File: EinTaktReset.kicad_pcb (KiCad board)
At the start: 2 copper layers, 34 parts, among them P10 CONN_01X01, P11 CONN_01X01, P12 CONN_01X01, P13 CONN_01X01, P14 CONN_01X01, P15 CONN_01X01, P2 CONN_01X01, P3 CONN_01X01, P4 CONN_02X10, P5 CONN_01X01, P6 CONN_01X01, P7 CONN_01X01, P8 CONN_01X01, P9 CONN_01X01, U2 74540En, U3 74HCT541_PWR

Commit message: footprinting EintaktReset3
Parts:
- added C3: 220 µ, Capacitors_ThroughHole:CP_Radial_D8.0mm_P3.50mm, F.Cu at (224.3, 28.2)
- added C4: 220µ, Capacitors_ThroughHole:CP_Radial_D8.0mm_P3.50mm, F.Cu at (233.4, 28.2)
- added C5: 10n, Capacitors_ThroughHole:C_Disc_D3.0mm_W1.6mm_P2.50mm, F.Cu at (206.4, 32.6)
- added D2: LED, LEDs:LED_D5.0mm, F.Cu at (200.4, 34.5)
- added DROT1: LED, LEDs:LED_D3.0mm, F.Cu at (250.3, 25.9)
- added P1: CONN_02X10, Pin_Headers:Pin_Header_Straight_2x10_Pitch2.00mm, F.Cu at (214.3, 3.02)
- added RV1: POT, Potentiometers:Potentiometer_Trimmer_Piher_PT-10v5_Horizontal_Px5.0mm_Py5.0mm, F.Cu at (213.3, 34.0)
- added SW10: SPST, tg_foodprint:eintakt_tg_SW_CuK_JS202011CQN_DPDT_Straight, F.Cu at (317.0, 11.1)
- added SW11: SPST, tg_foodprint:eintakt_tg_SW_CuK_JS202011CQN_DPDT_Straight, F.Cu at (325.2, 4.77)
- added SW12: SPST, tg_foodprint:eintakt_tg_SW_CuK_JS202011CQN_DPDT_Straight, F.Cu at (317.0, 17.4)
- added SW13: SPST, tg_foodprint:eintakt_tg_SW_CuK_JS202011CQN_DPDT_Straight, F.Cu at (325.2, 11.1)
- added SW5: SPST, tg_foodprint:eintakt_tg_SW_CuK_JS202011CQN_DPDT_Straight, F.Cu at (308.9, 4.77)
- added SW6: SWITCH_INV, Buttons_Switches_ThroughHole:SW_TH_Tactile_Omron_B3F-10xx, F.Cu at (241.1, 25.0)
- added SW7: SPST, tg_foodprint:eintakt_tg_SW_CuK_JS202011CQN_DPDT_Straight, F.Cu at (308.9, 11.1)
- added SW8: SPST, tg_foodprint:eintakt_tg_SW_CuK_JS202011CQN_DPDT_Straight, F.Cu at (317.0, 4.77)
- added SW9: SPST, tg_foodprint:eintakt_tg_SW_CuK_JS202011CQN_DPDT_Straight, F.Cu at (308.9, 17.4)
- added U1: 74LS132, Housings_DIP:DIP-14_W7.62mm_Socket_LongPads, F.Cu at (222.2, 3.29)
- added U10: 74LS00, Housings_DIP:DIP-14_W7.62mm_Socket_LongPads, F.Cu at (255.6, 3.29)
- added U4: 74LS32, Housings_DIP:DIP-20_W7.62mm_Socket_LongPads, F.Cu at (200.4, 3.29)
- added U5: 74LS00, Housings_DIP:DIP-14_W7.62mm_Socket_LongPads, F.Cu at (276.8, 3.29)
- added U6: 74LS132, Housings_DIP:DIP-14_W7.62mm_Socket_LongPads, F.Cu at (287.9, 3.29)
- added U8: 74LS32, Housings_DIP:DIP-14_W7.62mm_Socket_LongPads, F.Cu at (233.3, 3.29)
- added U9: 74LS32, Housings_DIP:DIP-14_W7.62mm_Socket_LongPads, F.Cu at (244.5, 3.29)

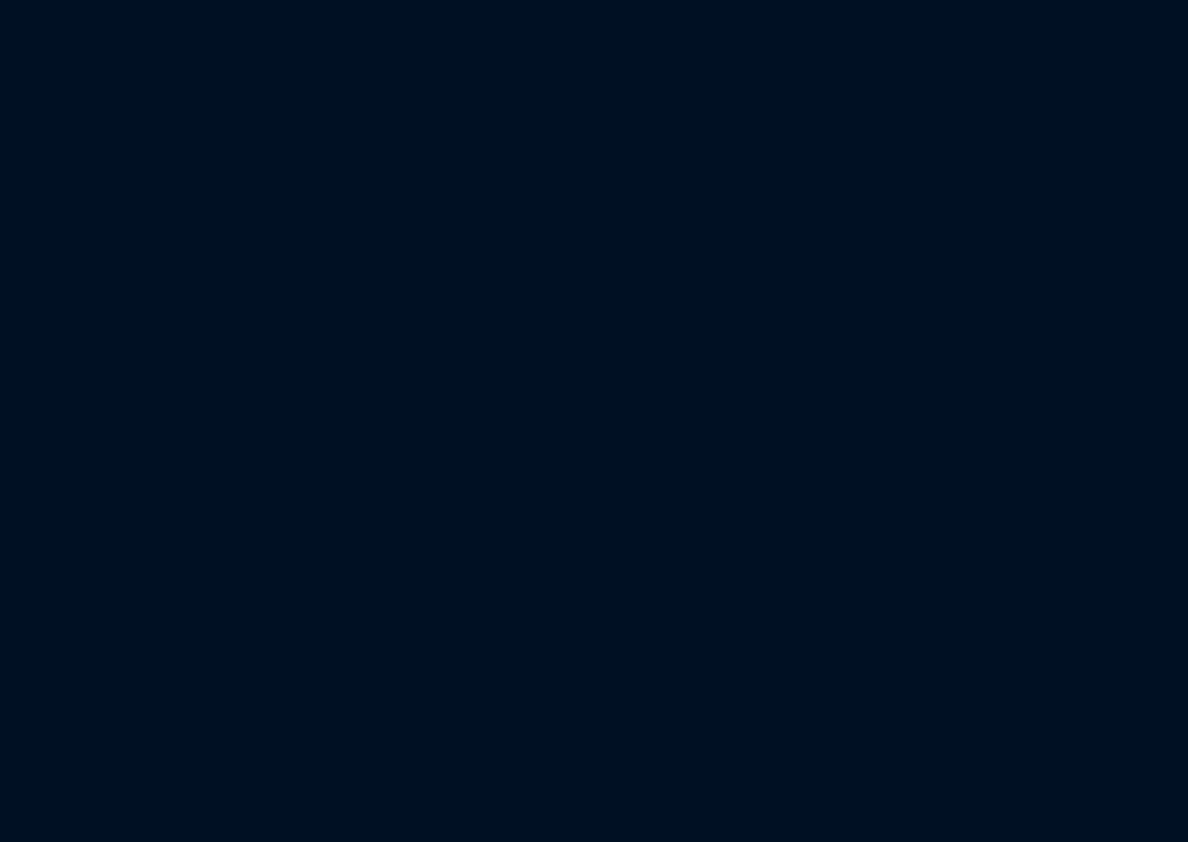
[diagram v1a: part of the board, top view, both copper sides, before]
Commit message: footprint IC1 ls624 VCO 14 pin
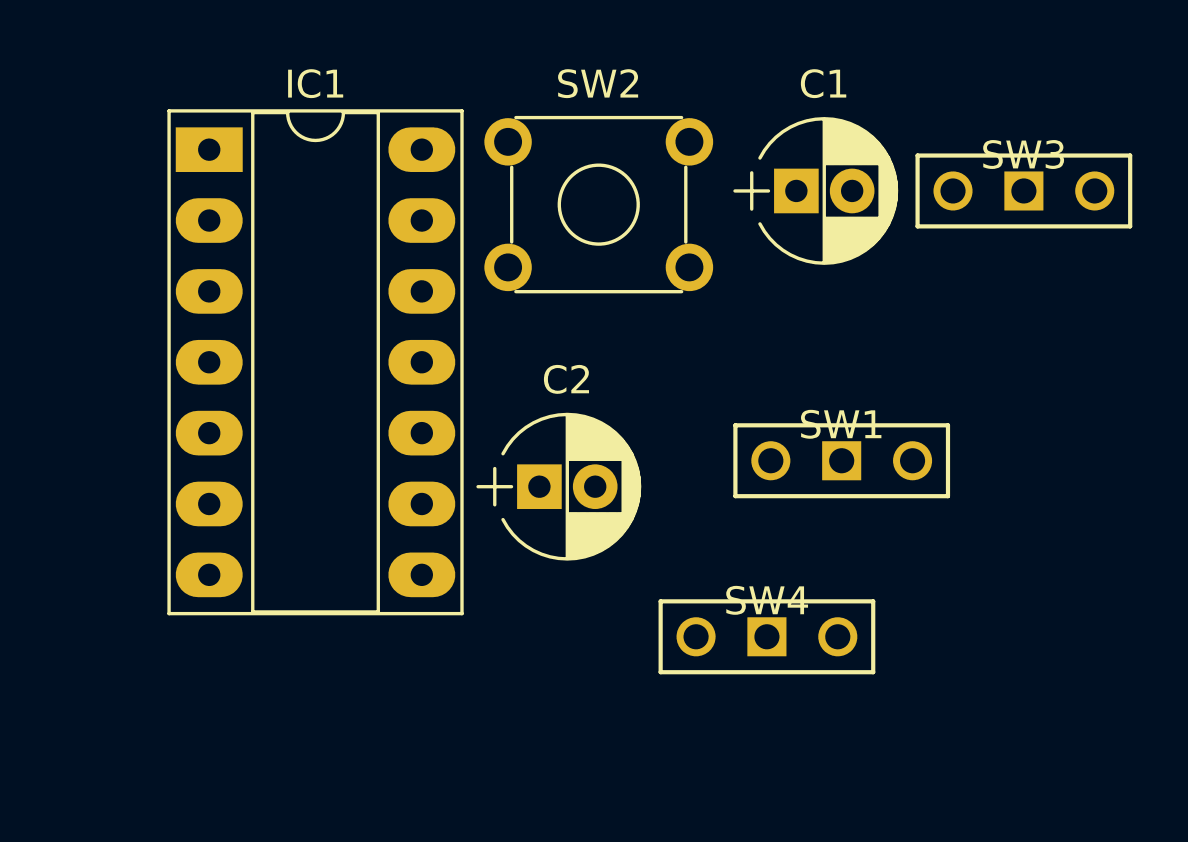
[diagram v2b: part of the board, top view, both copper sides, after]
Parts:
- added C1: 47µ, Capacitors_ThroughHole:CP_Radial_D5.0mm_P2.00mm, F.Cu at (364.6, 4.77)
- added C2: 10 µ, Capacitors_ThroughHole:CP_Radial_D5.0mm_P2.00mm, F.Cu at (355.4, 15.4)
- added IC1: 74LS624, Housings_DIP:DIP-14_W7.62mm_Socket_LongPads, F.Cu at (343.6, 3.29)
- added SW1: SPST, tg_foodprint:eintakt_tg_SW_CuK_JS202011CQN_DPDT_Straight, F.Cu at (363.7, 14.4)
- added SW2: SWITCH_INV, Buttons_Switches_ThroughHole:SW_TH_Tactile_Omron_B3F-10xx, F.Cu at (354.3, 3.01)
- added SW3: SPST, tg_foodprint:eintakt_tg_SW_CuK_JS202011CQN_DPDT_Straight, F.Cu at (370.3, 4.77)
- added SW4: SPST, tg_foodprint:eintakt_tg_SW_CuK_JS202011CQN_DPDT_Straight, F.Cu at (361.0, 20.7)

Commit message: footprint d1 smal diode do35 added
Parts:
- added D1: D, Diodes_ThroughHole:D_DO-35_SOD27_P7.62mm_Horizontal, F.Cu at (388.2, 3.02)
- moved P4 50.6 mm to (38.1, 54.6)
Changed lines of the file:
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@@
     (tracks 0)
     (zones 0)
-    (modules 64)
+    (modules 65)
     (nets 63)
   )
@@
   )
   (module Connect:1pin (layer F.Cu)
-    (at 36.468333 4.0055)
+    (at 38.1 54.61)
     (descr "module 1 pin (ou trou mecanique de percage)")
     (tags DEV)
@@
       (rotate (xyz 0 0 0))
     )
+  )
+  (module Diodes_ThroughHole:D_DO-35_SOD27_P7.62mm_Horizontal (layer F.Cu)
+    (at 388.158347 3.0175)
+    (descr "D, DO-35_SOD27 series, Axial, Horizontal, pin pitch=7.62mm, , length*diameter=4*2mm^2, , http://www.diodes.com/_files/packages/DO-35.pdf")
+    (tags "D DO-35_SOD27 series Axial Horizontal pin pitch 7.62mm  length 4mm diameter 2mm")
+    (fp_text reference D1 (at 3.81 -2.06) (layer F.SilkS)
+      (effects (font (size 1 1) (thickness 0.15)))
+    )
+    (fp_text value D (at 3.81 2.06) (layer F.Fab)
+      (effects (font (size 1 1) (thickness 0.15)))
+    )
+    (fp_line (start 8.7 -1.35) (end -1.05 -1.35) (layer F.CrtYd) (width 0.05))
+    (fp_line (start 8.7 1.35) (end 8.7 -1.35) (layer F.CrtYd) (width 0.05))
+    (fp_line (start -1.05 1.35) (end 8.7 1.35) (layer F.CrtYd) (width 0.05))
+    (fp_line (start -1.05 -1.35) (end -1.05 1.35) (layer F.CrtYd) (width 0.05))
+    (fp_line (start 2.41 -1.06) (end 2.41 1.06) (layer F.SilkS) (width 0.12))
+    (fp_line (start 6.64 0) (end 5.87 0) (layer F.SilkS) (width 0.12))
+    (fp_line (start 0.98 0) (end 1.75 0) (layer F.SilkS) (width 0.12))
+    (fp_line (start 5.87 -1.06) (end 1.75 -1.06) (layer F.SilkS) (width 0.12))
+    (fp_line (start 5.87 1.06) (end 5.87 -1.06) (layer F.SilkS) (width 0.12))
+    (fp_line (start 1.75 1.06) (end 5.87 1.06) (layer F.SilkS) (width 0.12))
+    (fp_line (start 1.75 -1.06) (end 1.75 1.06) (layer F.SilkS) (width 0.12))
+    (fp_line (start 2.41 -1) (end 2.41 1) (layer F.Fab) (width 0.1))
+    (fp_line (start 7.62 0) (end 5.81 0) (layer F.Fab) (width 0.1))
+    (fp_line (start 0 0) (end 1.81 0) (layer F.Fab) (width 0.1))
+    (fp_line (start 5.81 -1) (end 1.81 -1) (layer F.Fab) (width 0.1))
+    (fp_line (start 5.81 1) (end 5.81 -1) (layer F.Fab) (width 0.1))
+    (fp_line (start 1.81 1) (end 5.81 1) (layer F.Fab) (width 0.1))
+    (fp_line (start 1.81 -1) (end 1.81 1) (layer F.Fab) (width 0.1))
+    (fp_text user %R (at 3.81 0) (layer F.Fab)
+      (effects (font (size 1 1) (thickness 0.15)))
+    )
+    (pad 2 thru_hole oval (at 7.62 0) (size 1.6 1.6) (drill 0.8) (layers *.Cu *.Mask)
+      (net 41 "Net-(D1-Pad2)"))
+    (pad 1 thru_hole rect (at 0 0) (size 1.6 1.6) (drill 0.8) (layers *.Cu *.Mask)
+      (net 13 VCC))
+    (model ${KISYS3DMOD}/Diodes_THT.3dshapes/D_DO-35_SOD27_P7.62mm_Horizontal.wrl
+      (at (xyz 0 0 0))
+      (scale (xyz 0.393701 0.393701 0.393701))
+      (rotate (xyz 0 0 0))
+    )

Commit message: ic1 vco lib problem solved
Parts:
- IC1: footprint Housings_DIP:DIP-14_W7.62mm_Socket_LongPads -> Pin_Headers:Pin_Header_Straight_2x10_Pitch2.00mm
- P4: footprint Connect:1pin -> Pin_Headers:Pin_Header_Straight_2x10_Pitch2.00mm
- U4: footprint Housings_DIP:DIP-20_W7.62mm_Socket_LongPads -> Housings_DIP:DIP-14_W7.62mm_Socket_LongPads
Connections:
- IC1 pad 3: (no net) -> Net-(C5-Pad2)
- IC1 pad 7: GND -> Net-(IC1-Pad7)
- IC1 pad 9: VCC -> Net-(IC1-Pad9)

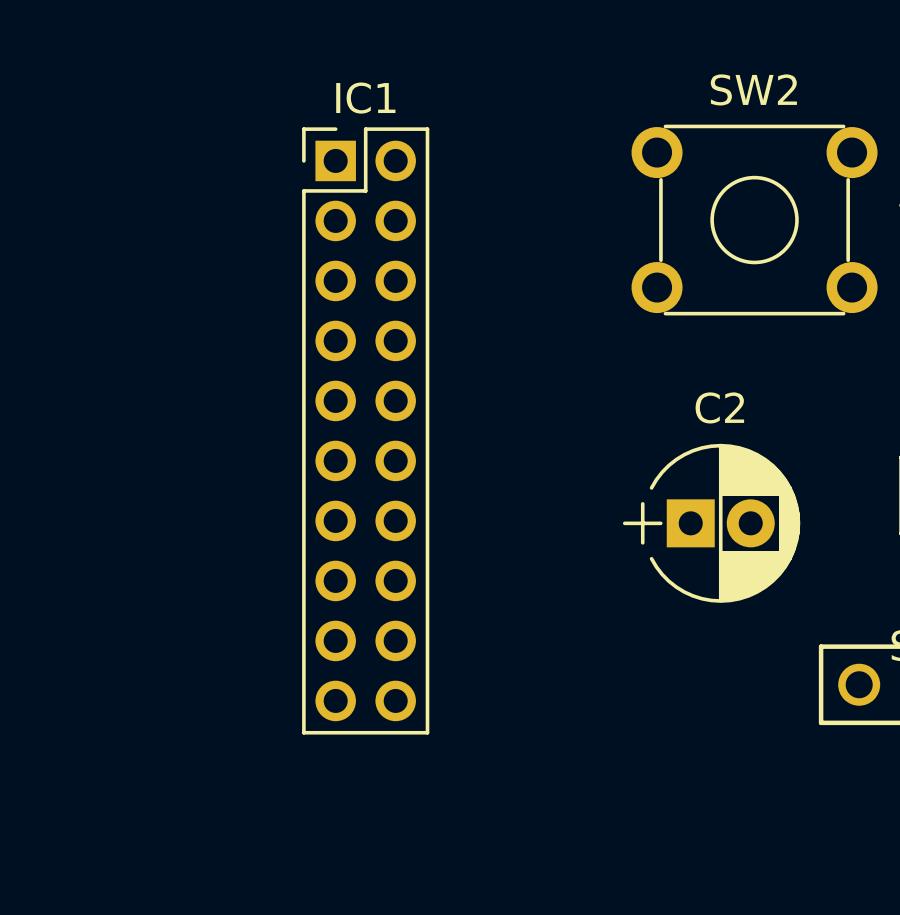
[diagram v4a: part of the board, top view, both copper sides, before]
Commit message: falsches gehäuse ic1 vco
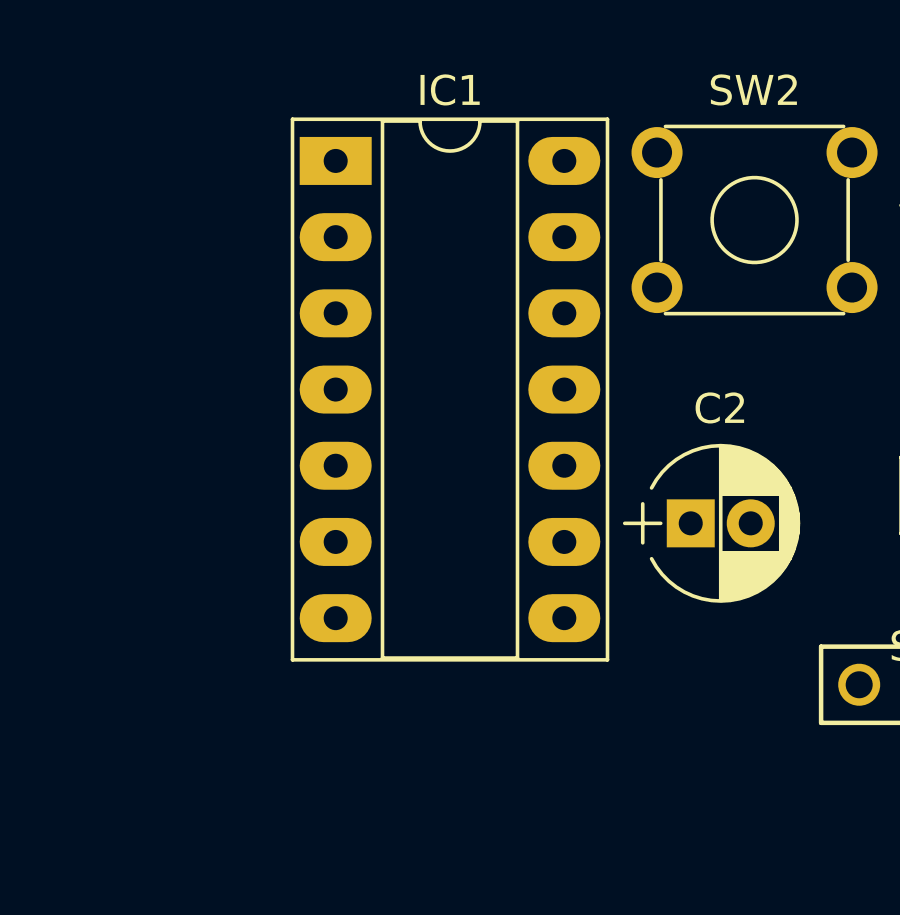
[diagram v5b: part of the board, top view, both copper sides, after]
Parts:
- IC1: footprint Pin_Headers:Pin_Header_Straight_2x10_Pitch2.00mm -> Housings_DIP:DIP-14_W7.62mm_Socket_LongPads
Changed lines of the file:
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@@
     )
   )
-  (module Pin_Headers:Pin_Header_Straight_2x10_Pitch2.00mm (layer F.Cu)
+  (module Housings_DIP:DIP-14_W7.62mm_Socket_LongPads (layer F.Cu)
     (at 343.598345 3.2875)
-    (descr "Through hole straight pin header, 2x10, 2.00mm pitch, double rows")
-    (tags "Through hole pin header THT 2x10 2.00mm double row")
-    (fp_text reference IC1 (at 1 -2.06) (layer F.SilkS)
+    (descr "14-lead though-hole mounted DIP package, row spacing 7.62 mm (300 mils), Socket, LongPads")
+    (tags "THT DIP DIL PDIP 2.54mm 7.62mm 300mil Socket LongPads")
+    (fp_text reference IC1 (at 3.81 -2.33) (layer F.SilkS)
       (effects (font (size 1 1) (thickness 0.15)))
     )
-    (fp_text value 74LS624 (at 1 20.06) (layer F.Fab)
+    (fp_text value 74LS624 (at 3.81 17.57) (layer F.Fab)
       (effects (font (size 1 1) (thickness 0.15)))
     )
-    (fp_text user %R (at 1 9 90) (layer F.Fab)
+    (fp_text user %R (at 3.81 7.62) (layer F.Fab)
       (effects (font (size 1 1) (thickness 0.15)))
     )
-    (fp_line (start 3.5 -1.5) (end -1.5 -1.5) (layer F.CrtYd) (width 0.05))
-    (fp_line (start 3.5 19.5) (end 3.5 -1.5) (layer F.CrtYd) (width 0.05))
-    (fp_line (start -1.5 19.5) (end 3.5 19.5) (layer F.CrtYd) (width 0.05))
-    (fp_line (start -1.5 -1.5) (end -1.5 19.5) (layer F.CrtYd) (width 0.05))
-    (fp_line (start -1.06 -1.06) (end 0 -1.06) (layer F.SilkS) (width 0.12))
-    (fp_line (start -1.06 0) (end -1.06 -1.06) (layer F.SilkS) (width 0.12))
-    (fp_line (start 1 -1.06) (end 3.06 -1.06) (layer F.SilkS) (width 0.12))
-    (fp_line (start 1 1) (end 1 -1.06) (layer F.SilkS) (width 0.12))
-    (fp_line (start -1.06 1) (end 1 1) (layer F.SilkS) (width 0.12))
-    (fp_line (start 3.06 -1.06) (end 3.06 19.06) (layer F.SilkS) (width 0.12))
-    (fp_line (start -1.06 1) (end -1.06 19.06) (layer F.SilkS) (width 0.12))
-    (fp_line (start -1.06 19.06) (end 3.06 19.06) (layer F.SilkS) (width 0.12))
-    (fp_line (start -1 0) (end 0 -1) (layer F.Fab) (width 0.1))
-    (fp_line (start -1 19) (end -1 0) (layer F.Fab) (width 0.1))
-    (fp_line (start 3 19) (end -1 19) (layer F.Fab) (width 0.1))
-    (fp_line (start 3 -1) (end 3 19) (layer F.Fab) (width 0.1))
-    (fp_line (start 0 -1) (end 3 -1) (layer F.Fab) (width 0.1))
-    (pad 20 thru_hole oval (at 2 18) (size 1.35 1.35) (drill 0.8) (layers *.Cu *.Mask))
-    (pad 19 thru_hole oval (at 0 18) (size 1.35 1.35) (drill 0.8) (layers *.Cu *.Mask))
-    (pad 18 thru_hole oval (at 2 16) (size 1.35 1.35) (drill 0.8) (layers *.Cu *.Mask))
-    (pad 17 thru_hole oval (at 0 16) (size 1.35 1.35) (drill 0.8) (layers *.Cu *.Mask))
-    (pad 16 thru_hole oval (at 2 14) (size 1.35 1.35) (drill 0.8) (layers *.Cu *.Mask))
-    (pad 15 thru_hole oval (at 0 14) (size 1.35 1.35) (drill 0.8) (layers *.Cu *.Mask))
-    (pad 14 thru_hole oval (at 2 12) (size 1.35 1.35) (drill 0.8) (layers *.Cu *.Mask)
+    (fp_line (start 9.15 -1.6) (end -1.55 -1.6) (layer F.CrtYd) (width 0.05))
+    (fp_line (start 9.15 16.85) (end 9.15 -1.6) (layer F.CrtYd) (width 0.05))
+    (fp_line (start -1.55 16.85) (end 9.15 16.85) (layer F.CrtYd) (width 0.05))
+    (fp_line (start -1.55 -1.6) (end -1.55 16.85) (layer F.CrtYd) (width 0.05))
+    (fp_line (start 9.06 -1.39) (end -1.44 -1.39) (layer F.SilkS) (width 0.12))
+    (fp_line (start 9.06 16.63) (end 9.06 -1.39) (layer F.SilkS) (width 0.12))
+    (fp_line (start -1.44 16.63) (end 9.06 16.63) (layer F.SilkS) (width 0.12))
+    (fp_line (start -1.44 -1.39) (end -1.44 16.63) (layer F.SilkS) (width 0.12))
+    (fp_line (start 6.06 -1.33) (end 4.81 -1.33) (layer F.SilkS) (width 0.12))
+    (fp_line (start 6.06 16.57) (end 6.06 -1.33) (layer F.SilkS) (width 0.12))
+    (fp_line (start 1.56 16.57) (end 6.06 16.57) (layer F.SilkS) (width 0.12))
+    (fp_line (start 1.56 -1.33) (end 1.56 16.57) (layer F.SilkS) (width 0.12))
+    (fp_line (start 2.81 -1.33) (end 1.56 -1.33) (layer F.SilkS) (width 0.12))
+    (fp_line (start 8.89 -1.33) (end -1.27 -1.33) (layer F.Fab) (width 0.1))
+    (fp_line (start 8.89 16.57) (end 8.89 -1.33) (layer F.Fab) (width 0.1))
+    (fp_line (start -1.27 16.57) (end 8.89 16.57) (layer F.Fab) (width 0.1))
+    (fp_line (start -1.27 -1.33) (end -1.27 16.57) (layer F.Fab) (width 0.1))
+    (fp_line (start 0.635 -0.27) (end 1.635 -1.27) (layer F.Fab) (width 0.1))
+    (fp_line (start 0.635 16.51) (end 0.635 -0.27) (layer F.Fab) (width 0.1))
+    (fp_line (start 6.985 16.51) (end 0.635 16.51) (layer F.Fab) (width 0.1))
+    (fp_line (start 6.985 -1.27) (end 6.985 16.51) (layer F.Fab) (width 0.1))
+    (fp_line (start 1.635 -1.27) (end 6.985 -1.27) (layer F.Fab) (width 0.1))
+    (fp_arc (start 3.81 -1.33) (end 2.81 -1.33) (angle -180) (layer F.SilkS) (width 0.12))
+    (pad 14 thru_hole oval (at 7.62 0) (size 2.4 1.6) (drill 0.8) (layers *.Cu *.Mask)
       (net 13 VCC))
-    (pad 13 thru_hole oval (at 0 12) (size 1.35 1.35) (drill 0.8) (layers *.Cu *.Mask)
+    (pad 7 thru_hole oval (at 0 15.24) (size 2.4 1.6) (drill 0.8) (layers *.Cu *.Mask)
+      (net 63 "Net-(IC1-Pad7)"))
+    (pad 13 thru_hole oval (at 7.62 2.54) (size 2.4 1.6) (drill 0.8) (layers *.Cu *.Mask)
       (net 51 "Net-(IC1-Pad13)"))
-    (pad 12 thru_hole oval (at 2 10) (size 1.35 1.35) (drill 0.8) (layers *.Cu *.Mask))
-    (pad 11 thru_hole oval (at 0 10) (size 1.35 1.35) (drill 0.8) (layers *.Cu *.Mask))
-    (pad 10 thru_hole oval (at 2 8) (size 1.35 1.35) (drill 0.8) (layers *.Cu *.Mask))
-    (pad 9 thru_hole oval (at 0 8) (size 1.35 1.35) (drill 0.8) (layers *.Cu *.Mask)
+    (pad 6 thru_hole oval (at 0 12.7) (size 2.4 1.6) (drill 0.8) (layers *.Cu *.Mask)
+      (net 62 "Net-(IC1-Pad6)"))
+    (pad 12 thru_hole oval (at 7.62 5.08) (size 2.4 1.6) (drill 0.8) (layers *.Cu *.Mask))
+    (pad 5 thru_hole oval (at 0 10.16) (size 2.4 1.6) (drill 0.8) (layers *.Cu *.Mask)
+      (net 39 "Net-(4,7k3-Pad2)"))
+    (pad 11 thru_hole oval (at 7.62 7.62) (size 2.4 1.6) (drill 0.8) (layers *.Cu *.Mask))
+    (pad 4 thru_hole oval (at 0 7.62) (size 2.4 1.6) (drill 0.8) (layers *.Cu *.Mask)
+      (net 49 "Net-(C4-Pad2)"))
+    (pad 10 thru_hole oval (at 7.62 10.16) (size 2.4 1.6) (drill 0.8) (layers *.Cu *.Mask))
+    (pad 3 thru_hole oval (at 0 5.08) (size 2.4 1.6) (drill 0.8) (layers *.Cu *.Mask)
+      (net 50 "Net-(C5-Pad2)"))
+    (pad 9 thru_hole oval (at 7.62 12.7) (size 2.4 1.6) (drill 0.8) (layers *.Cu *.Mask)
       (net 64 "Net-(IC1-Pad9)"))
-    (pad 8 thru_hole oval (at 2 6) (size 1.35 1.35) (drill 0.8) (layers *.Cu *.Mask)
+    (pad 2 thru_hole oval (at 0 2.54) (size 2.4 1.6) (drill 0.8) (layers *.Cu *.Mask)
+      (net 40 "Net-(10k1-Pad1)"))
+    (pad 8 thru_hole oval (at 7.62 15.24) (size 2.4 1.6) (drill 0.8) (layers *.Cu *.Mask)
       (net 59 "Net-(IC1-Pad8)"))
-    (pad 7 thru_hole oval (at 0 6) (size 1.35 1.35) (drill 0.8) (layers *.Cu *.Mask)
-      (net 63 "Net-(IC1-Pad7)"))
-    (pad 6 thru_hole oval (at 2 4) (size 1.35 1.35) (drill 0.8) (layers *.Cu *.Mask)
-      (net 62 "Net-(IC1-Pad6)"))
-    (pad 5 thru_hole oval (at 0 4) (size 1.35 1.35) (drill 0.8) (layers *.Cu *.Mask)
-      (net 39 "Net-(4,7k3-Pad2)"))
-    (pad 4 thru_hole oval (at 2 2) (size 1.35 1.35) (drill 0.8) (layers *.Cu *.Mask)
-      (net 49 "Net-(C4-Pad2)"))
-    (pad 3 thru_hole oval (at 0 2) (size 1.35 1.35) (drill 0.8) (layers *.Cu *.Mask)
-      (net 50 "Net-(C5-Pad2)"))
-    (pad 2 thru_hole oval (at 2 0) (size 1.35 1.35) (drill 0.8) (layers *.Cu *.Mask)
-      (net 40 "Net-(10k1-Pad1)"))
-    (pad 1 thru_hole rect (at 0 0) (size 1.35 1.35) (drill 0.8) (layers *.Cu *.Mask)
+    (pad 1 thru_hole rect (at 0 0) (size 2.4 1.6) (drill 0.8) (layers *.Cu *.Mask)
       (net 12 GND))
-    (model ${KISYS3DMOD}/Pin_Headers.3dshapes/Pin_Header_Straight_2x10_Pitch2.00mm.wrl
+    (model ${KISYS3DMOD}/Housings_DIP.3dshapes/DIP-14_W7.62mm_Socket.wrl
       (at (xyz 0 0 0))
       (scale (xyz 1 1 1))
